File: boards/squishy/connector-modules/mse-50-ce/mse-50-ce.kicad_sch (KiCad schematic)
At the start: 14 parts, among them J1 SCSI PHY Mezz, J2 Conn_02x25_Odd_Even, J3 Conn_01x04, J4 Conn_02x34_Clockwise_Shield, J5 Conn_02x24_Clockwise_Shield, U1 M24C02-RMC

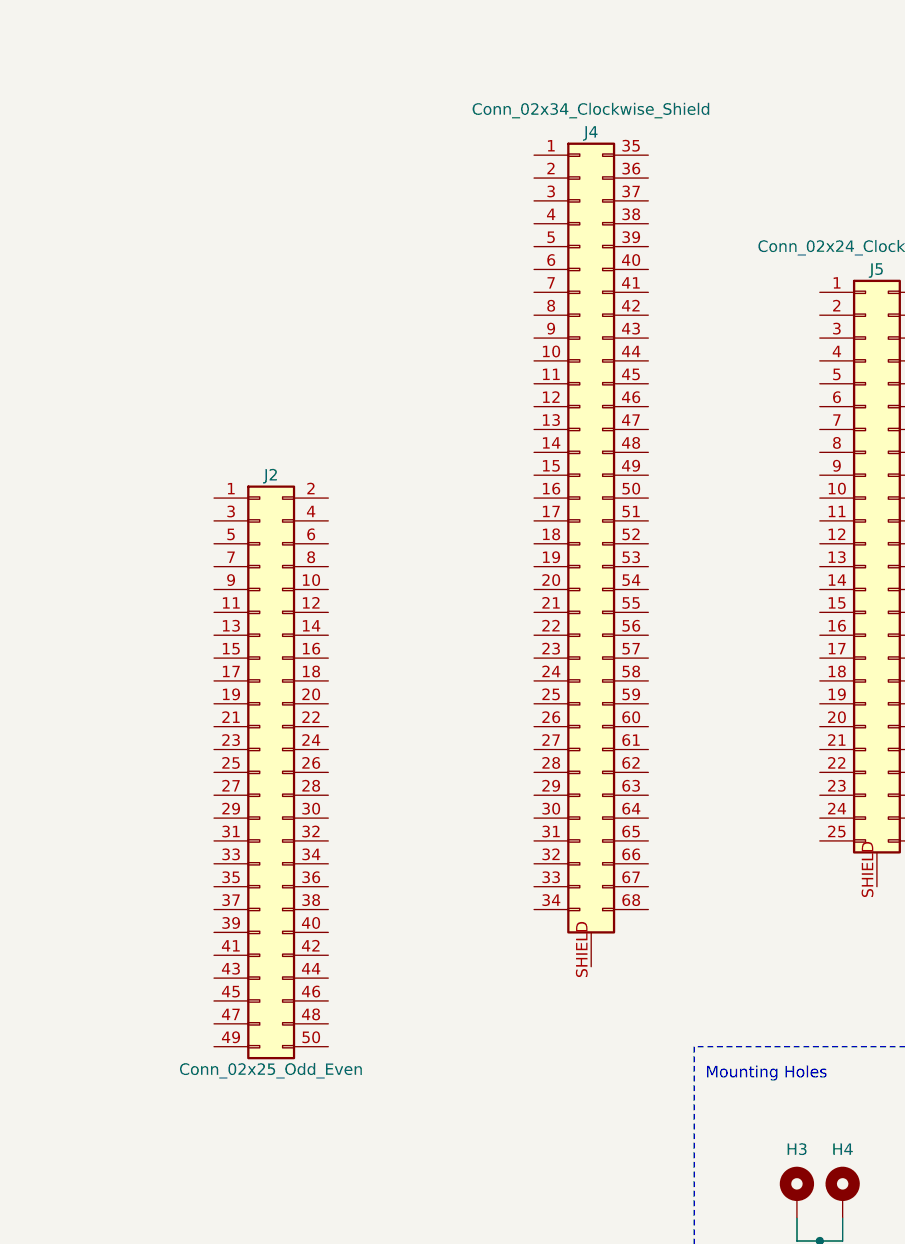
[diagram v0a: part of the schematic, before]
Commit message: squishy: connectors: Removed unneeded connector symbols in the given kicad schematics
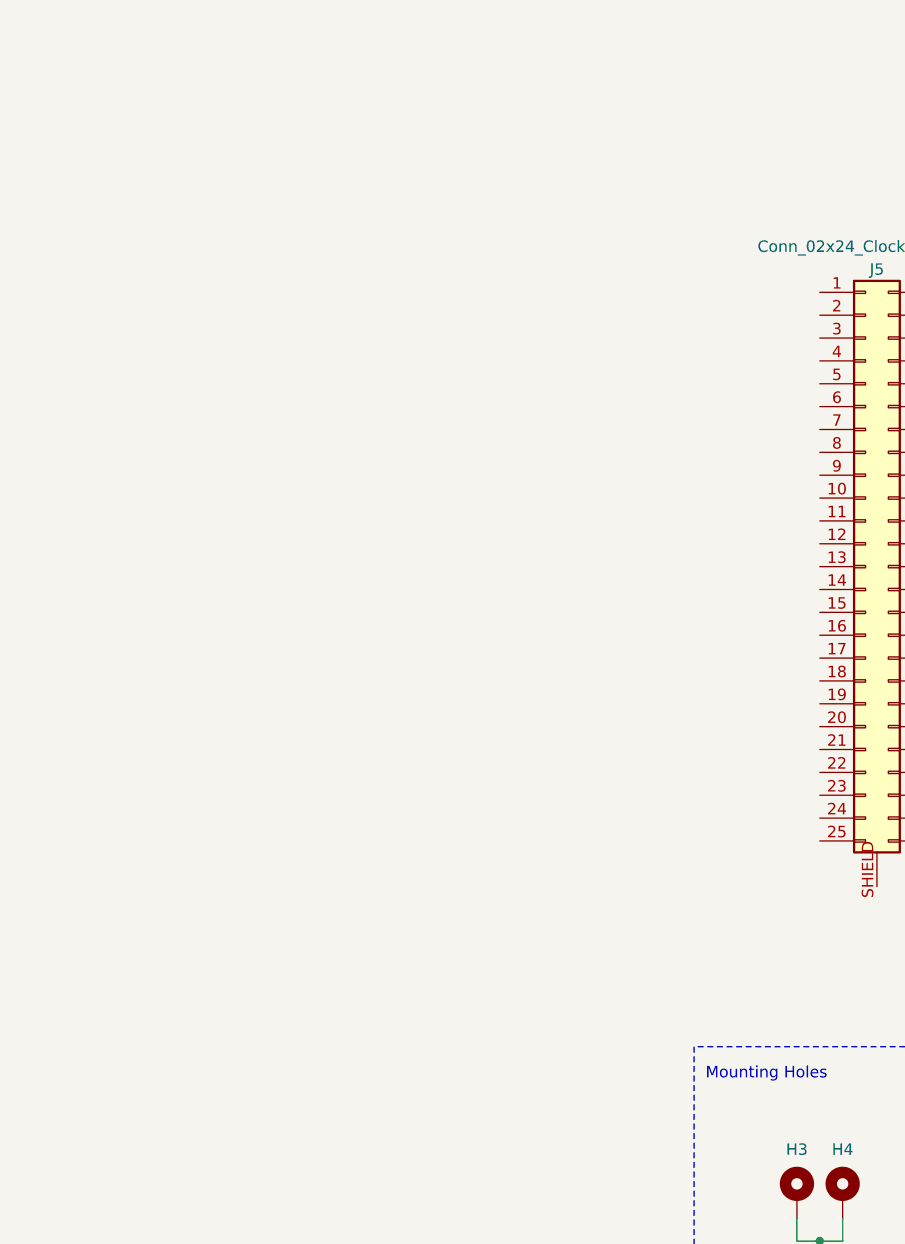
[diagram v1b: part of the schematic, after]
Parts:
- removed J2: Conn_02x25_Odd_Even, Connector_IDC:IDC-Header_2x25_P2.54mm_Horizontal, symbol Connector_Generic:Conn_02x25_Odd_Even
- removed J4: Conn_02x34_Clockwise_Shield, symbol lethalbit-connectors:Conn_02x34_Counter_Clockwise

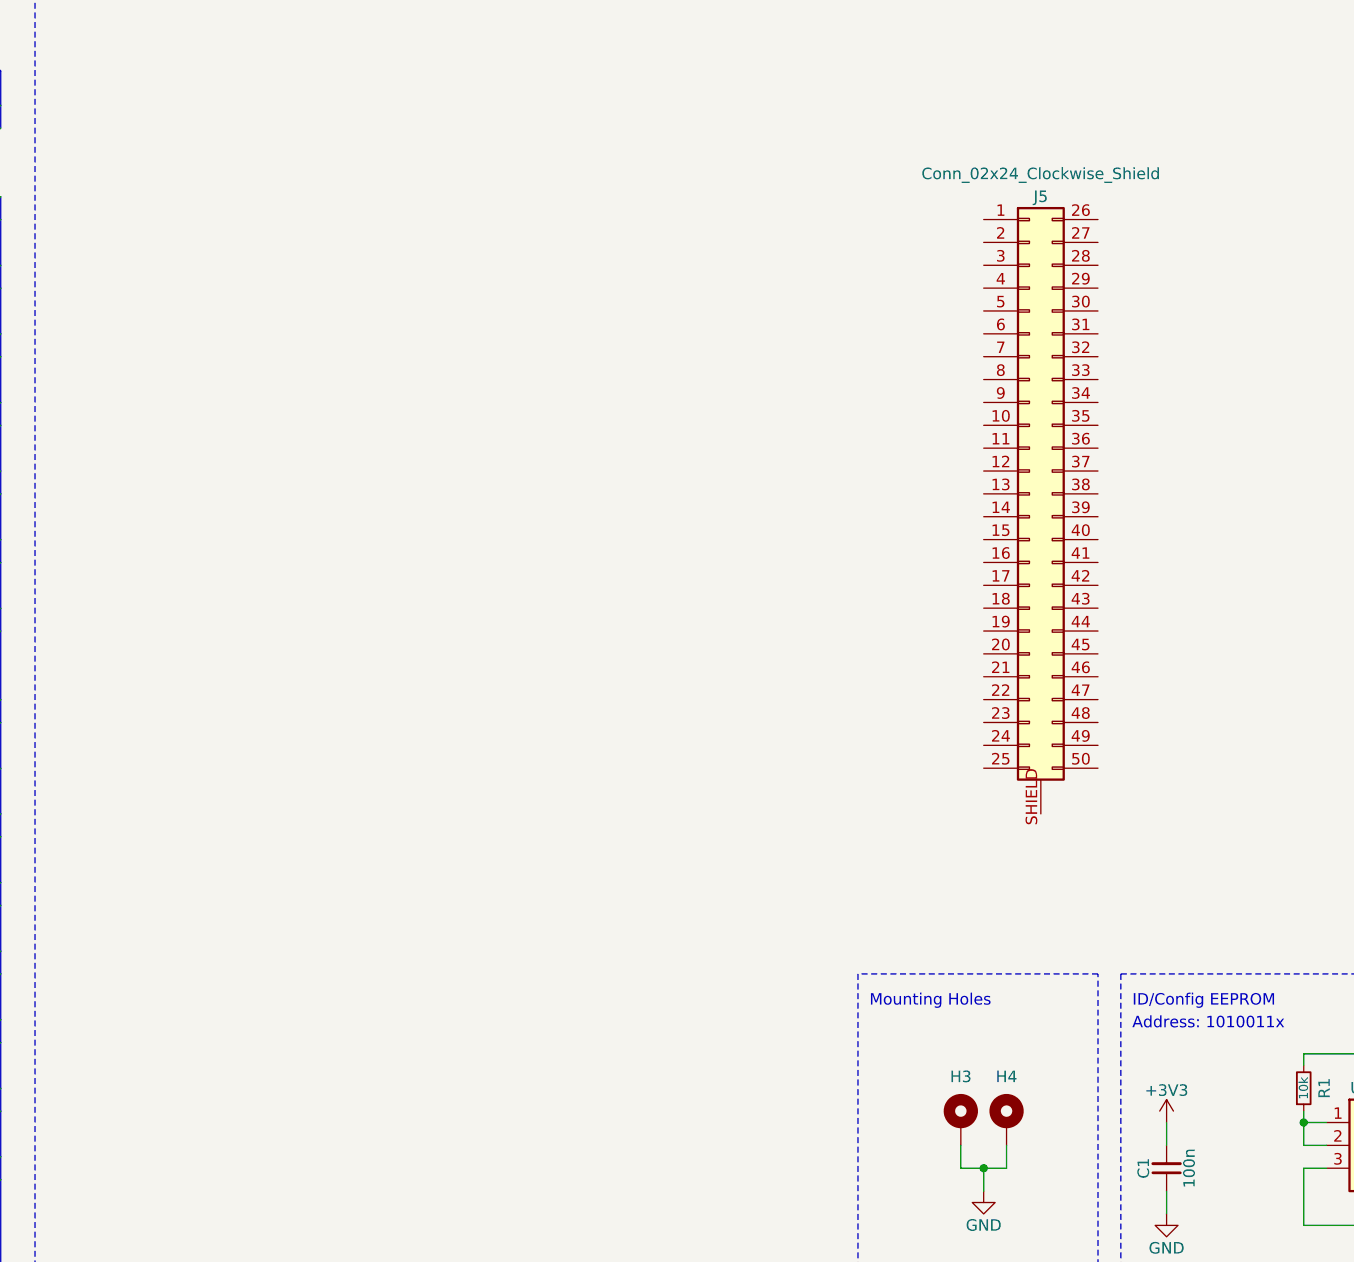
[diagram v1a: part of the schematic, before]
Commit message: squishy: connectors: hooked up mse-50-ce connector
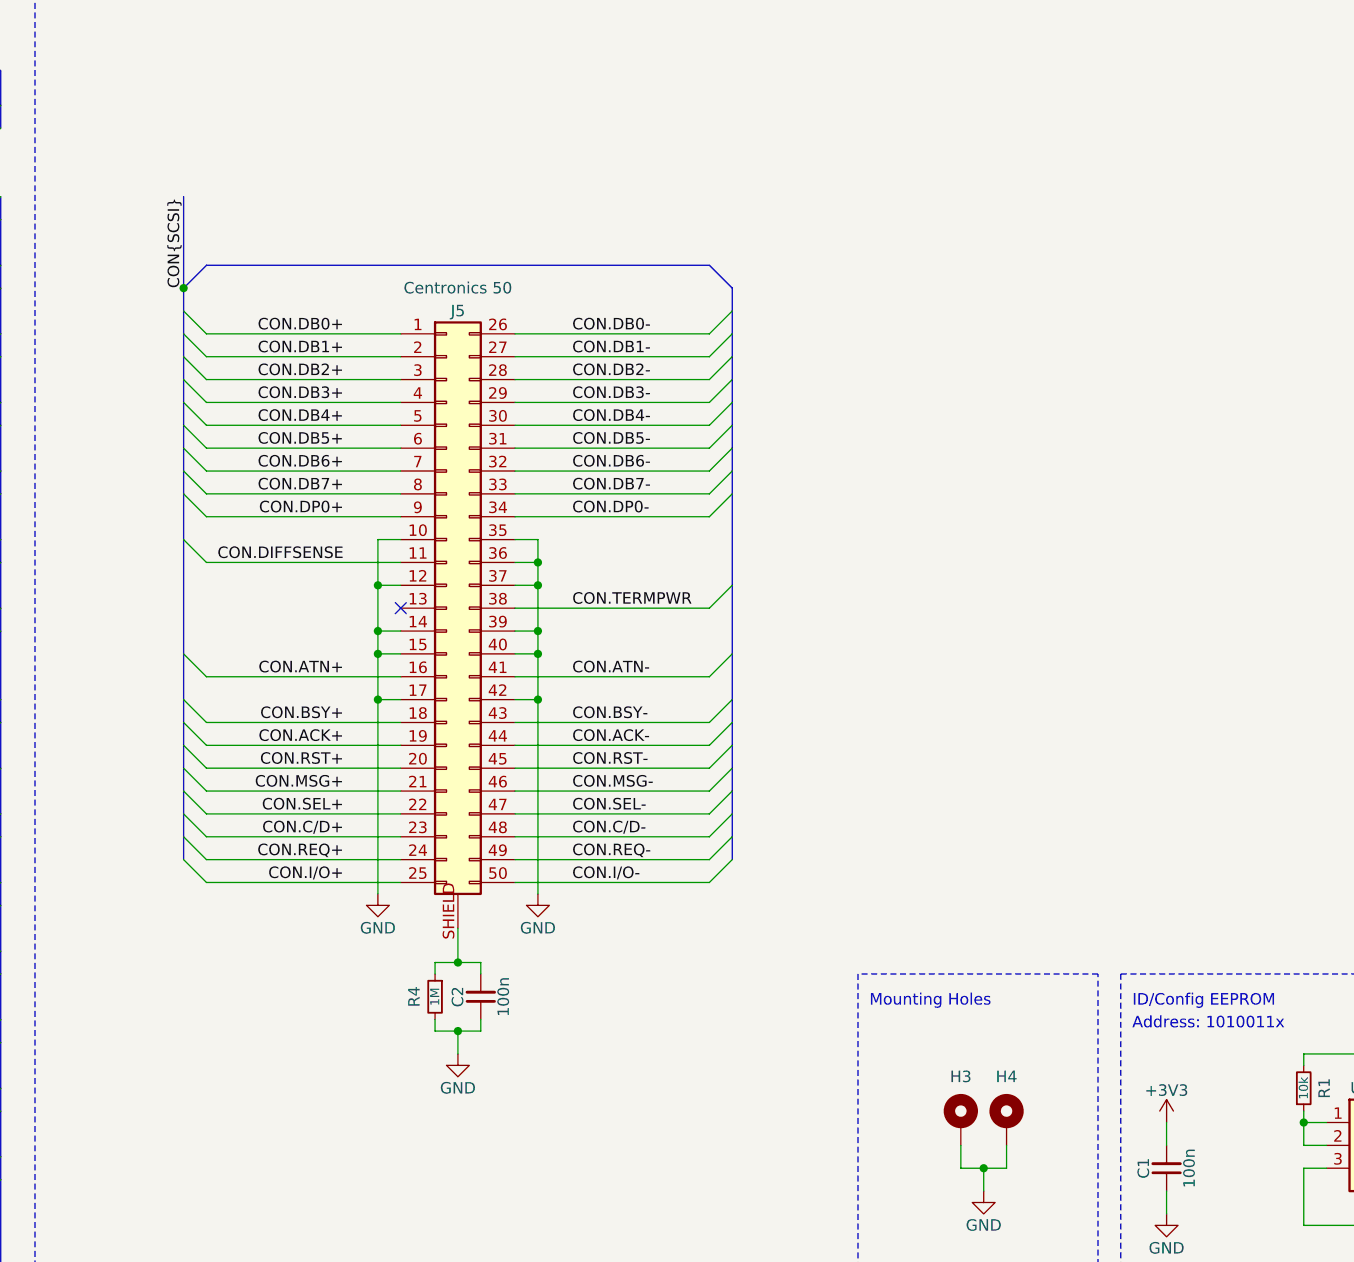
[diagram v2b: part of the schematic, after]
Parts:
- added C2: 100n, rhais_rcl:C0603, symbol Device:C_Small
- added R4: 1M, rhais_rcl:R0603, symbol Device:R_Small
- J5: value Conn_02x24_Clockwise_Shield -> Centronics 50; footprint (none) -> lethalbit-connectors:112-050-213R001
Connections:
- net CON.ACK+: now also J5.19 (Pin_19)
- net CON.ACK-: now also J5.44 (Pin_44)
- net CON.ATN+: now also J5.16 (Pin_16)
- net CON.ATN-: now also J5.41 (Pin_41)
- net CON.BSY+: now also J5.18 (Pin_18)
- net CON.BSY-: now also J5.43 (Pin_43)
- net CON.C/D+: now also J5.23 (Pin_23)
- net CON.C/D-: now also J5.48 (Pin_48)
- net CON.DB0+: now also J5.1 (Pin_1)
- net CON.DB0-: now also J5.26 (Pin_26)
- net CON.DB1+: now also J5.2 (Pin_2)
- net CON.DB1-: now also J5.27 (Pin_27)
- net CON.DB2+: now also J5.3 (Pin_3)
- net CON.DB2-: now also J5.28 (Pin_28)
- net CON.DB3+: now also J5.4 (Pin_4)
- net CON.DB3-: now also J5.29 (Pin_29)
- net CON.DB4+: now also J5.5 (Pin_5)
- net CON.DB4-: now also J5.30 (Pin_30)
- net CON.DB5+: now also J5.6 (Pin_6)
- net CON.DB5-: now also J5.31 (Pin_31)
- net CON.DB6+: now also J5.7 (Pin_7)
- net CON.DB6-: now also J5.32 (Pin_32)
- net CON.DB7+: now also J5.8 (Pin_8)
- net CON.DB7-: now also J5.33 (Pin_33)
- net CON.DIFFSENSE: now also J5.11 (Pin_11)
- net CON.DP0+: now also J5.9 (Pin_9)
- net CON.DP0-: now also J5.34 (Pin_34)
- net CON.I/O+: now also J5.25 (Pin_25)
- net CON.I/O-: now also J5.50 (Pin_50)
- net CON.MSG+: now also J5.21 (Pin_21)
- net CON.MSG-: now also J5.46 (Pin_46)
- net CON.REQ+: now also J5.24 (Pin_24)
- net CON.REQ-: now also J5.49 (Pin_49)
- net CON.RST+: now also J5.20 (Pin_20)
- net CON.RST-: now also J5.45 (Pin_45)
- net CON.SEL+: now also J5.22 (Pin_22)
- net CON.SEL-: now also J5.47 (Pin_47)
- net CON.TERMPWR: now also J5.38 (Pin_38)
- net GND: now also J5.10 (Pin_10), J5.12 (Pin_12), J5.14 (Pin_14), J5.15 (Pin_15), J5.17 (Pin_17), J5.35 (Pin_35), J5.36 (Pin_36), J5.37 (Pin_37), J5.39 (Pin_39), J5.40 (Pin_40), J5.42 (Pin_42), C2.1, R4.2
- net at J5.SHIELD: now also C2.2, R4.1
- no-connect marks 2 -> 3
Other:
- moved on the sheet: J5

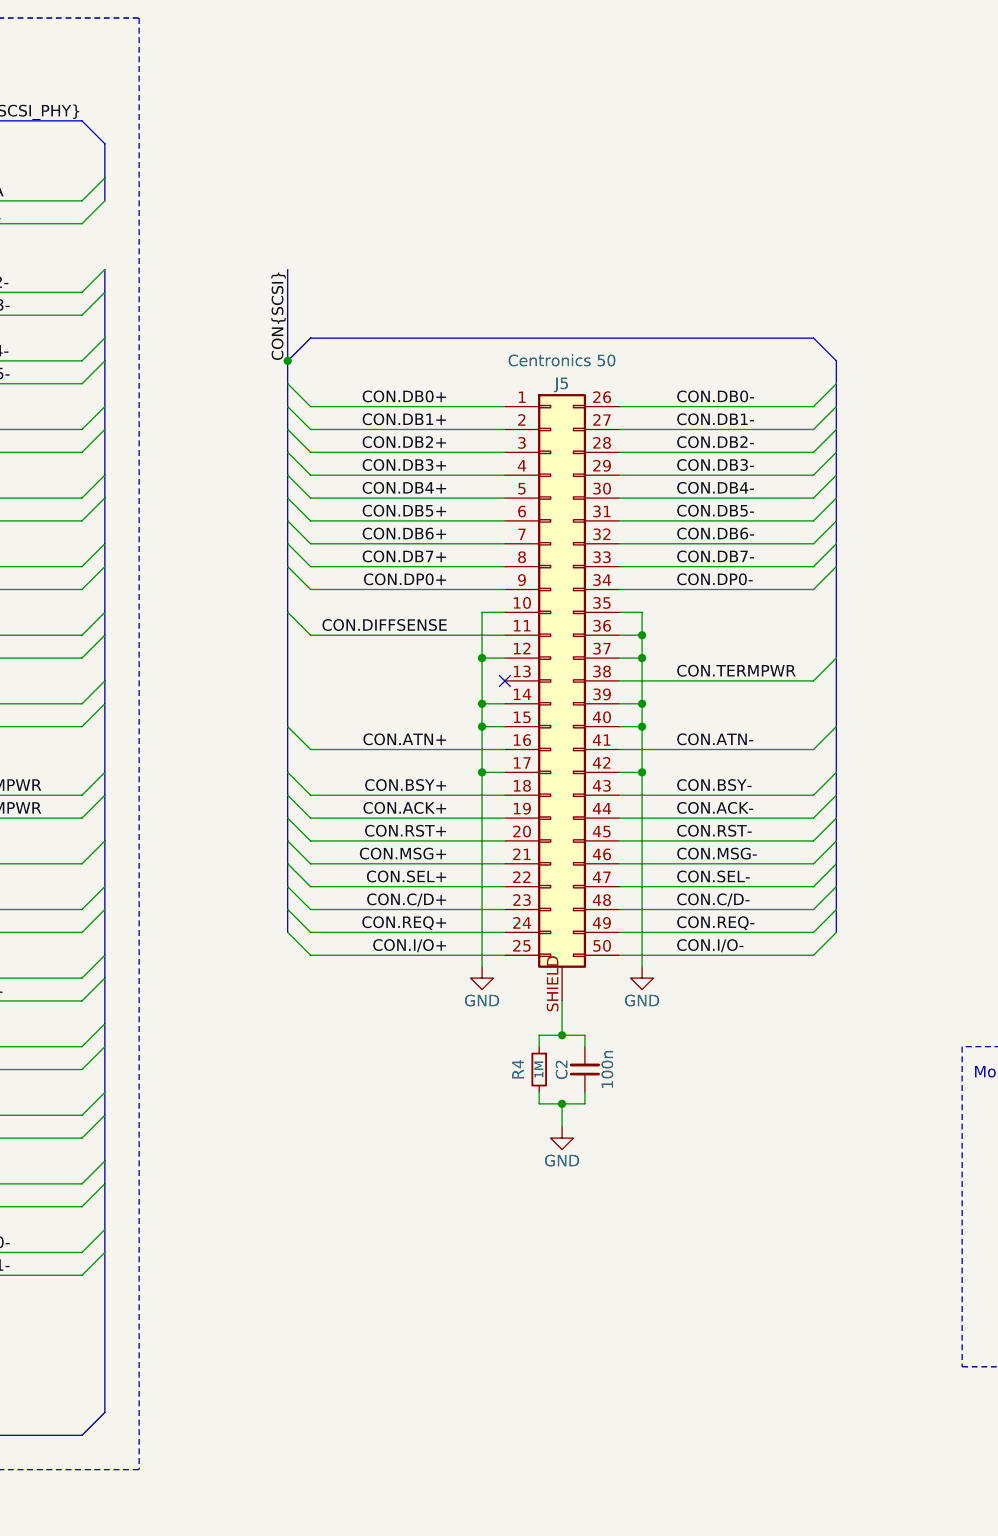
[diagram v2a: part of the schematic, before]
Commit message: squishy: connectors: Cleaned up and unified look/feel of connector schematics
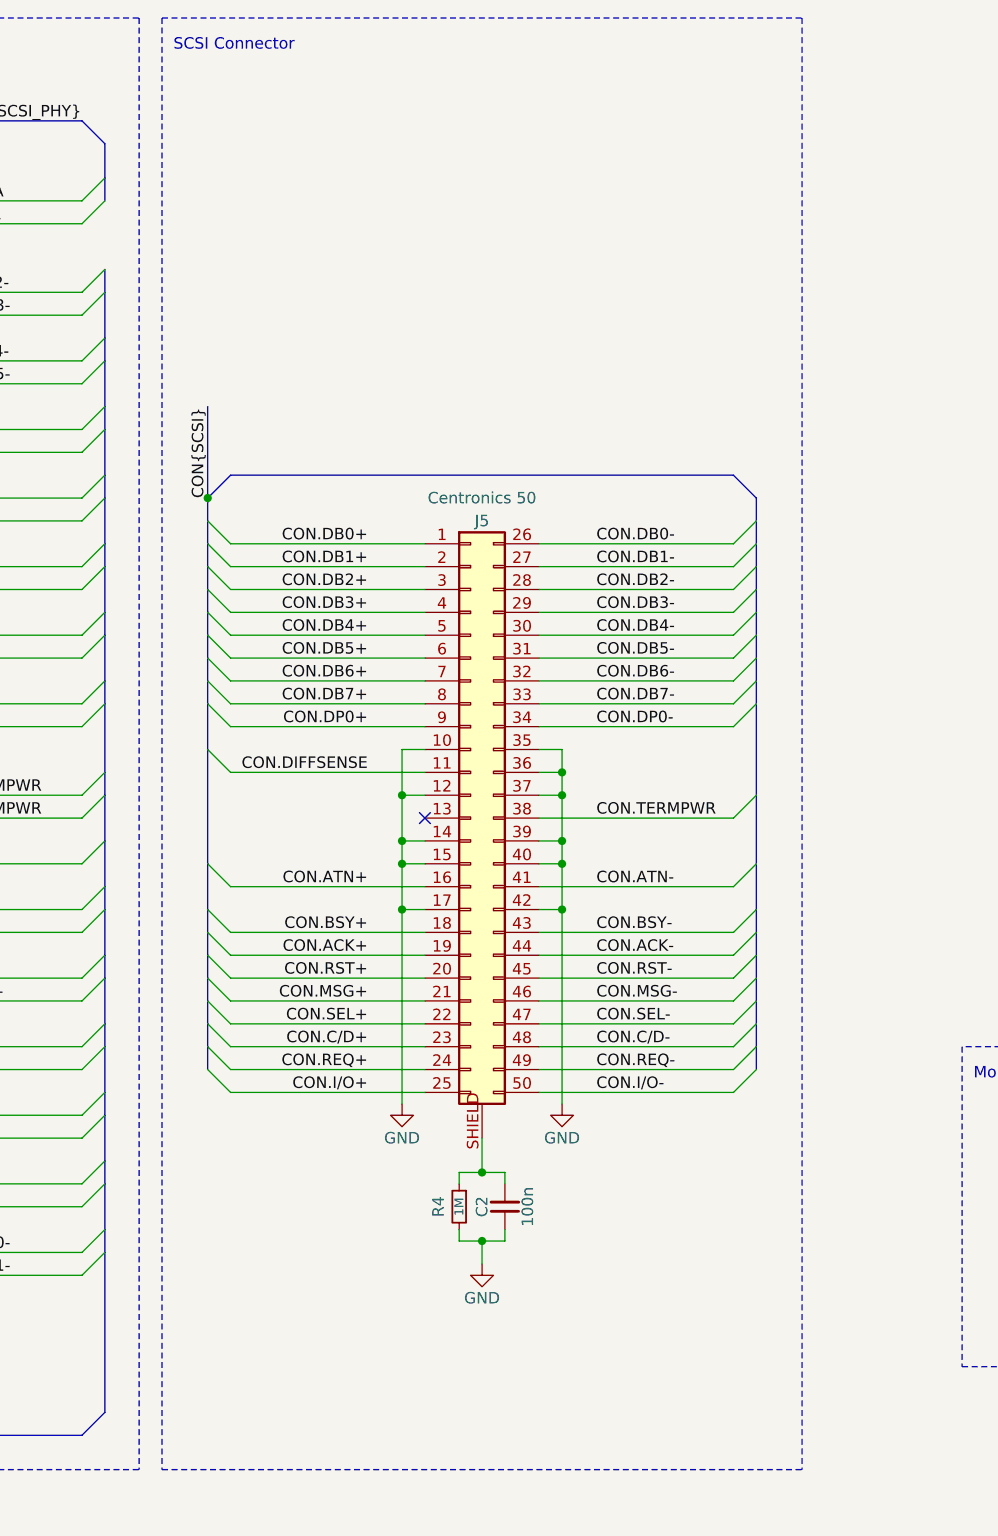
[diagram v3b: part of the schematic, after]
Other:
- note added: "SCSI Connector"
- moved on the sheet: C2, J5, R4

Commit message: squishy: connectors: updated schematic title blocks for connectors as appropriate
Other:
- title: Squishy -  ICD 50 -> Squishy -  SCSI LVD/MSE/SE Centronics 50 Connector Module
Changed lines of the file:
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@@
 	(paper "A4")
 	(title_block
-		(title "Squishy -  ICD 50")
-		(date "2024-08-22")
+		(title "Squishy -  SCSI LVD/MSE/SE Centronics 50 Connector Module")
+		(date "2024-09-17")
 		(rev "1")
 		(company "Shrine Maiden Heavy Industries")
